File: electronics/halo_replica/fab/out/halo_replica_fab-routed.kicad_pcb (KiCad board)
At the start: 4 copper layers, 30 x 30 mm, 45 parts, among them J1 VOICE COIL / SOUNDER, J2 NFC COIL 13.56MHz, J3 SWD (nRST SWDIO SWCLK GND VBA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, U1 nRF52832-QFAA-R, U2 MIC94090YC6 (0.5 uA, 1.5 A), U3 MX25R3235F 32Mb 1.65-3.6V, U4 SC7A20 3-axis, LGA-12, U5 MAX98357A class-D, TQFN-16, X1 32MHz 10ppm CL=8pF, X2 32.768kHz 20ppm CL=12.5pF

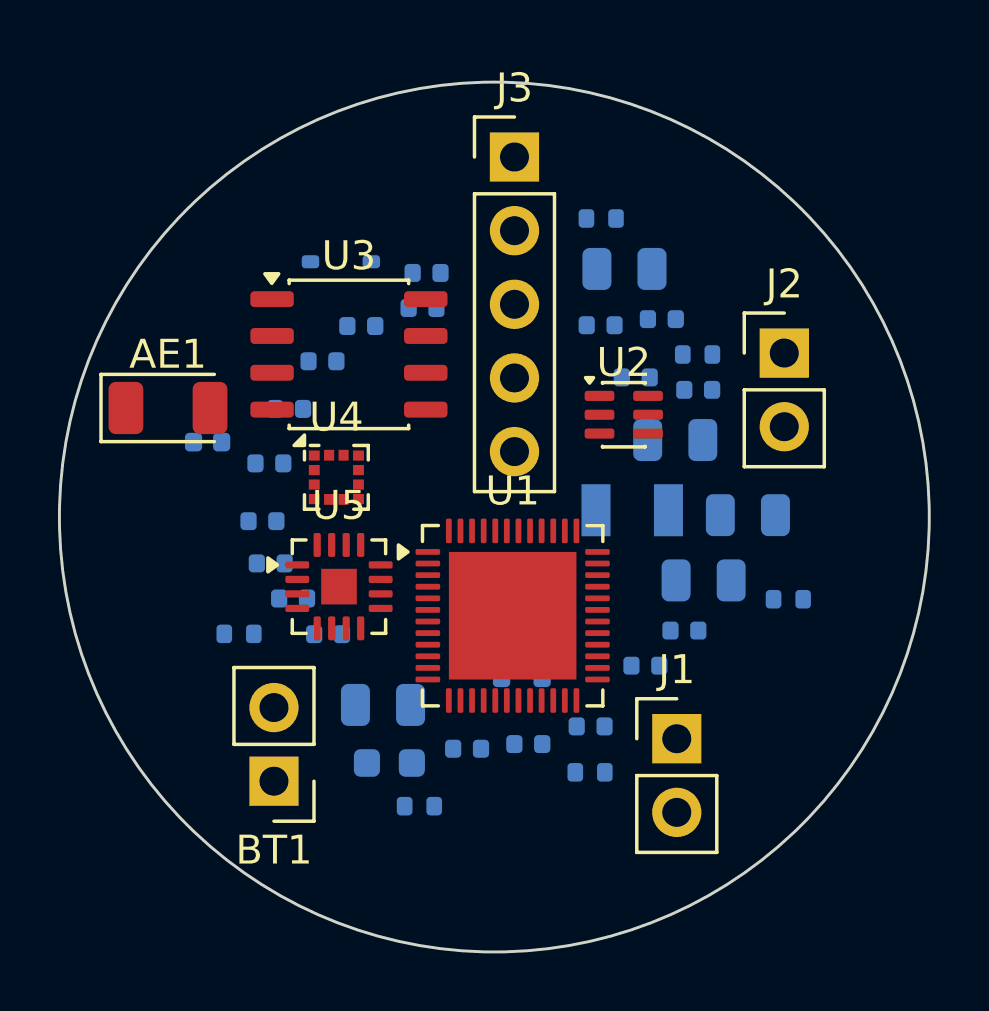
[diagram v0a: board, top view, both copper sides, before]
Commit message: fab: the board routes — 112 unconnected to 5, zero DRC errors
The board was never unroutable. It was unplaceable, and freerouting had been
saying so for hours in the only way it can: an identical score on four
consecutive completed passes.

  placement broken   -mp 100, 3502 s wall / 1913 s CPU  ->  no .ses at all
  placement fixed    -mp 3,     44.4 s                  ->  112 unconnected to 18
  placement fixed    -mp 30,   250.8 s                  ->  112 unconnected to 5

Routed board: 565 tracks, 58 vias, all four copper layers used (F.Cu 206,
B.Cu 236, In1 56, In2 67), 63 nets, 0 DRC errors, 77 silkscreen warnings.

DRC errors along the way, every number measured:
  135  parts off the board; rule tighter than the parts' own land patterns
   37  after the frame fix
   46  after the holder swap - WORSE, because the new small BT1 was still
       excluded from the relaxation, so J3 landed on it (16 shorting_items).
       A part the solver cannot see is a part everything else may sit on.
   15  after side-aware placement (the back face was empty on a 4-layer board)
    0  after correcting origin-vs-courtyard-centre, measured at 5.08 mm on a
       1x05 header whose origin is pin 1

Package verified end to end: 13 gerbers + Excellon + gbrjob + CPL (45
placements) + BOM (5 real LCSC codes, 20 blank, 0 prose) + ORDER-SETTINGS,
z_fabcheck exit 0.

Five nets remain unconnected and this does NOT claim a finished board.

Co-Authored-By: Claude Opus 5 (1M context) <noreply@anthropic.com>
Claude-Session: https://claude.ai/code/session_01JRY3feHovaK2VS3mL7infx
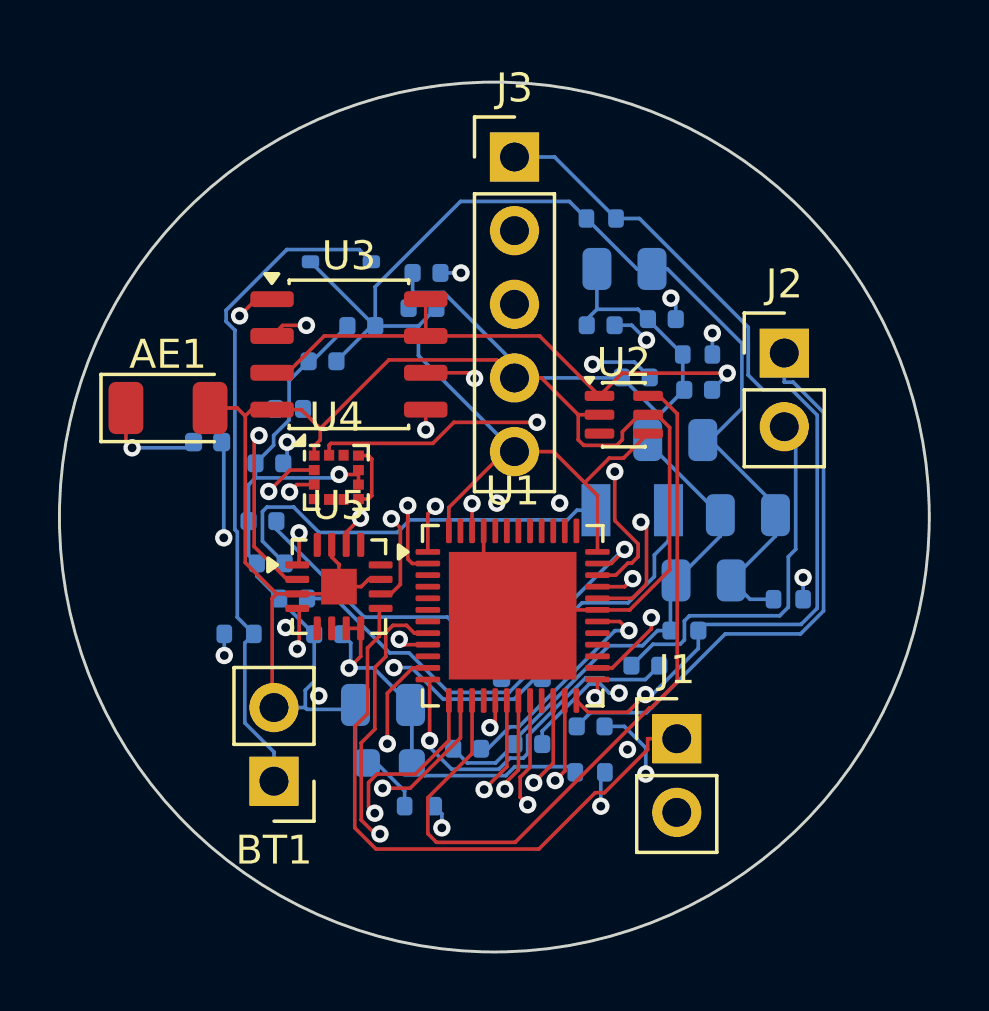
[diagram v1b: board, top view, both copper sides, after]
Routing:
- net GND: track 0.00 -> 117.8 mm, vias 0 -> 1
- net VBAT: track 0.00 -> 109.3 mm, vias 0 -> 3
- net ACC_SCL: track 0.00 -> 40.5 mm, vias 0 -> 3
- net ACC_SDA: track 0.00 -> 38.3 mm, vias 0 -> 4
- net XC1: track 0.00 -> 37.5 mm, vias 0 -> 3
- net nRESET: track 0.00 -> 32.1 mm, vias 0 -> 1
- net ANT_FEED: track 0.00 -> 28.2 mm, vias 0 -> 2
- net FLASH_PWR_EN: track 0.00 -> 26.7 mm
- net ANT_SOC: track 0.00 -> 26.6 mm, vias 0 -> 2
- net SPI_SCK: track 0.00 -> 26.1 mm, vias 0 -> 5
- net FLASH_nCS: track 0.00 -> 24.4 mm, vias 0 -> 2
- net AMP_GAIN: track 0.00 -> 23.9 mm, vias 0 -> 2
- net SPI_MISO: track 0.00 -> 23.3 mm, vias 0 -> 2
- net VBAT_RAW: track 0.00 -> 23.2 mm
- net SPK_N: track 0.00 -> 21.9 mm, vias 0 -> 1
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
